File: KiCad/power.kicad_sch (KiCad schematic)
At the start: 42 parts

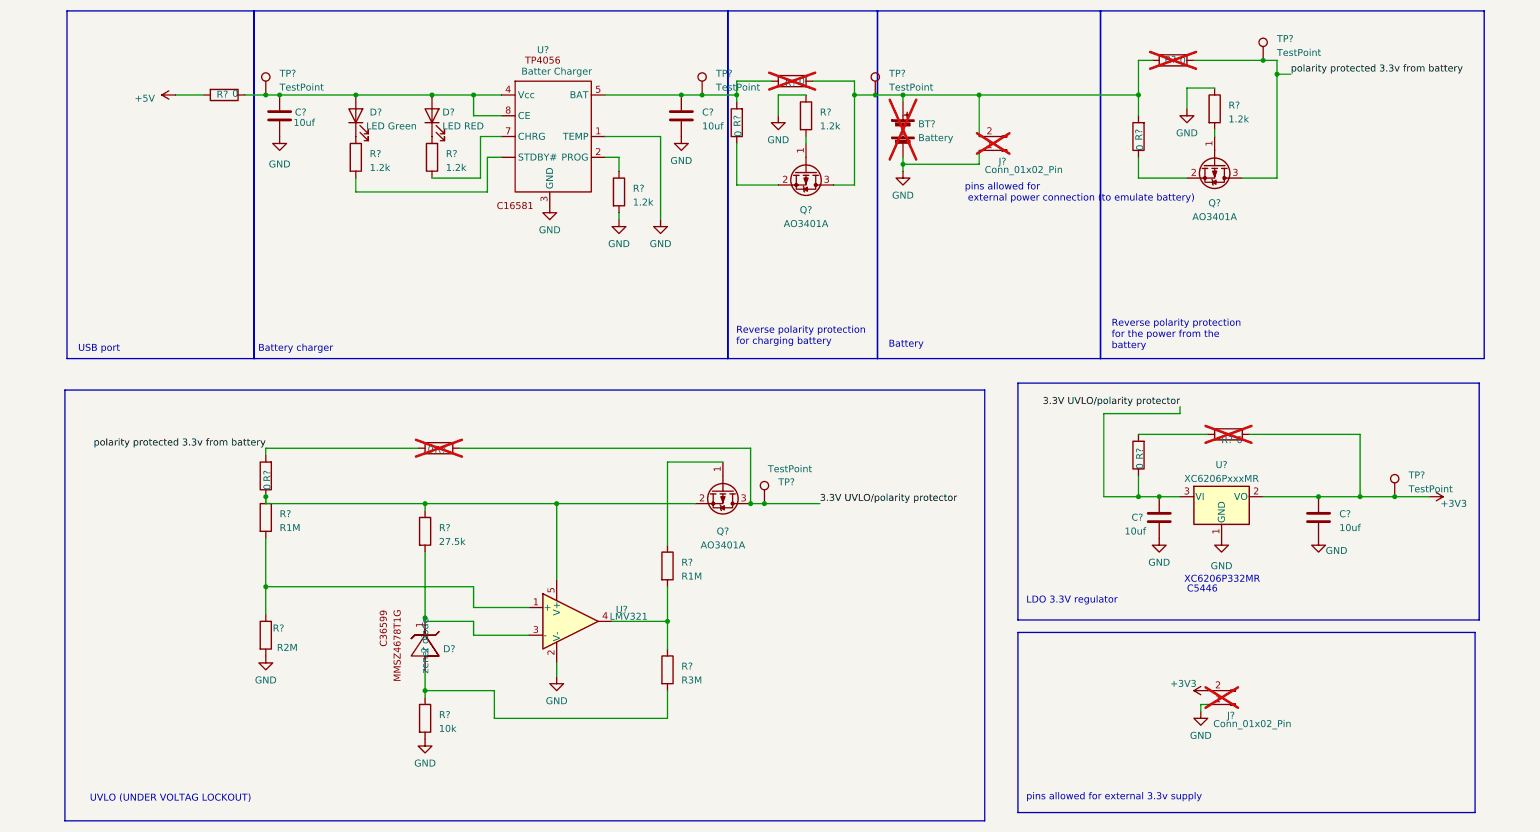
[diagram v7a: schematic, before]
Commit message: updated net labelling scheme on schematic, changed some port connections on microcontroller
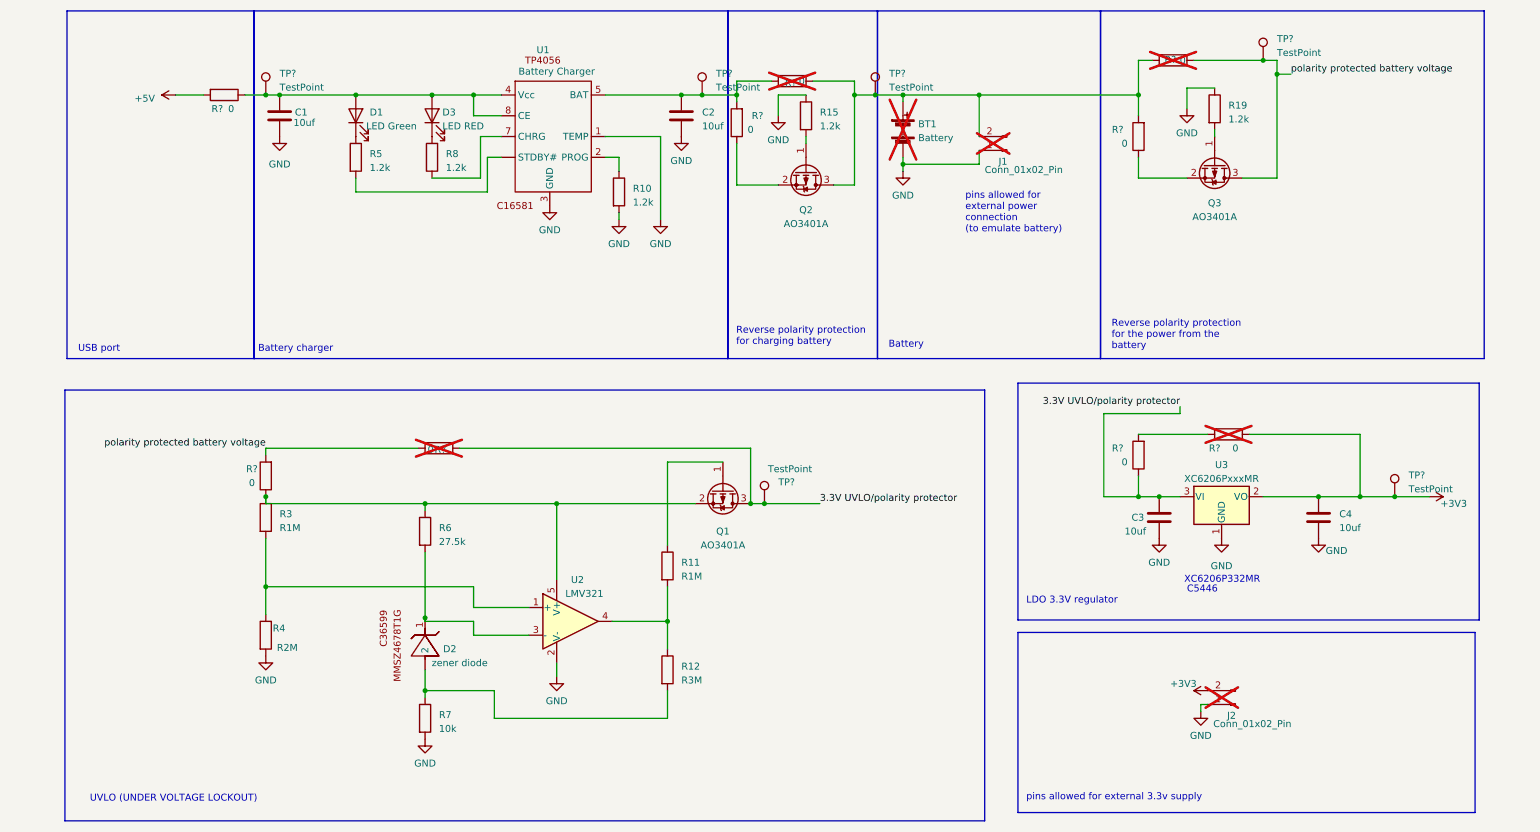
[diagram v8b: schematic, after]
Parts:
- U1: renamed from U?; value Batter Charger -> Battery Charger
- gave numbers to parts that had none: 26
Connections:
- net polarity protected 3.3v from battery renamed polarity protected battery voltage
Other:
- note added: "UVLO (UNDER VOLTAGE LOCKOUT)"
- note removed: "UVLO (UNDER VOLTAG LOCKOUT)"
